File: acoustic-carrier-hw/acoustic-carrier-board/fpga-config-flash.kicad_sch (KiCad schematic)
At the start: 20 parts, among them IC1 ECP5-BGA256, J701 Conn_01x10_Socket, J702 Conn_01x08_Socket, U701 W25Q128JVS, U702 W25Q128JVS

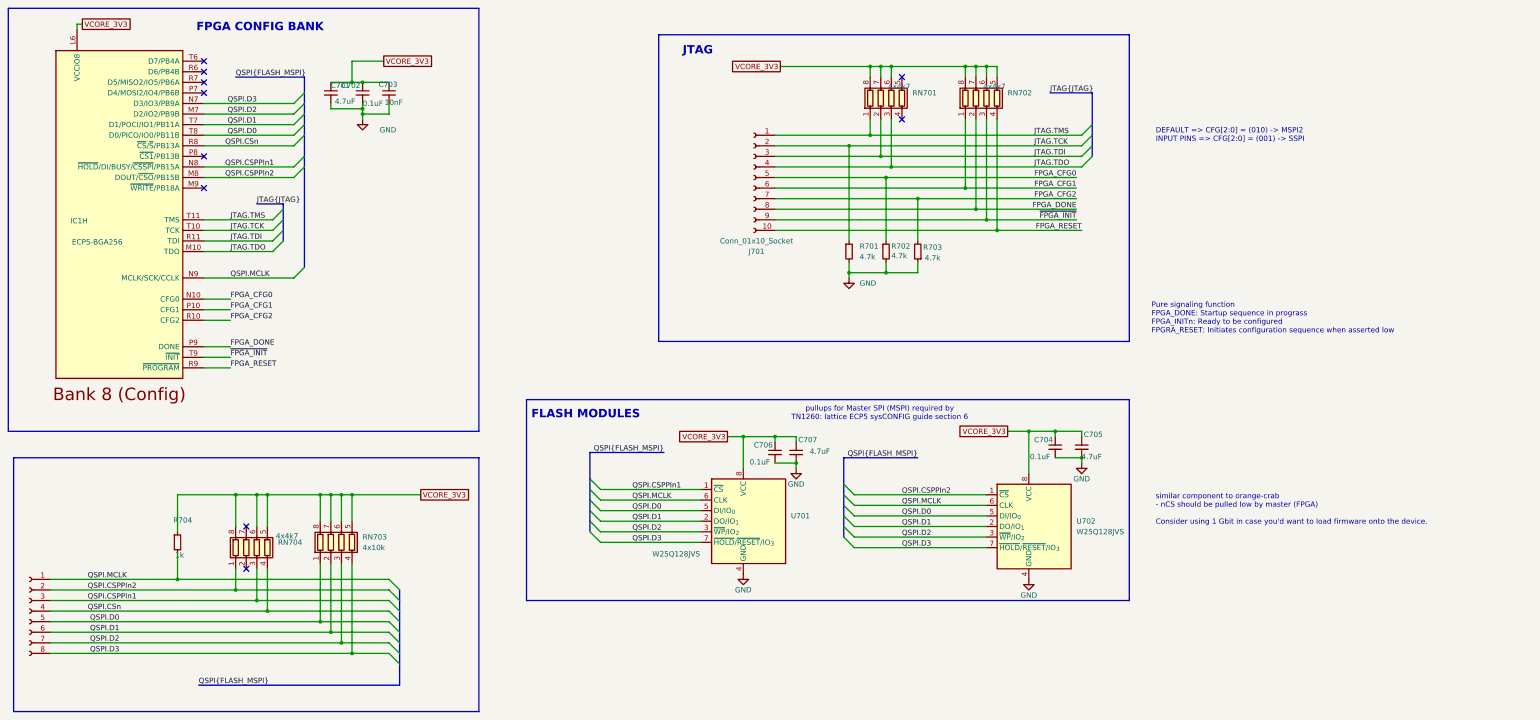
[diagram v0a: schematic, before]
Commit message: [carrier] Layout more or less complete (next) think about adding 6x2 connectors, and add extra pin signals to the connector for testing
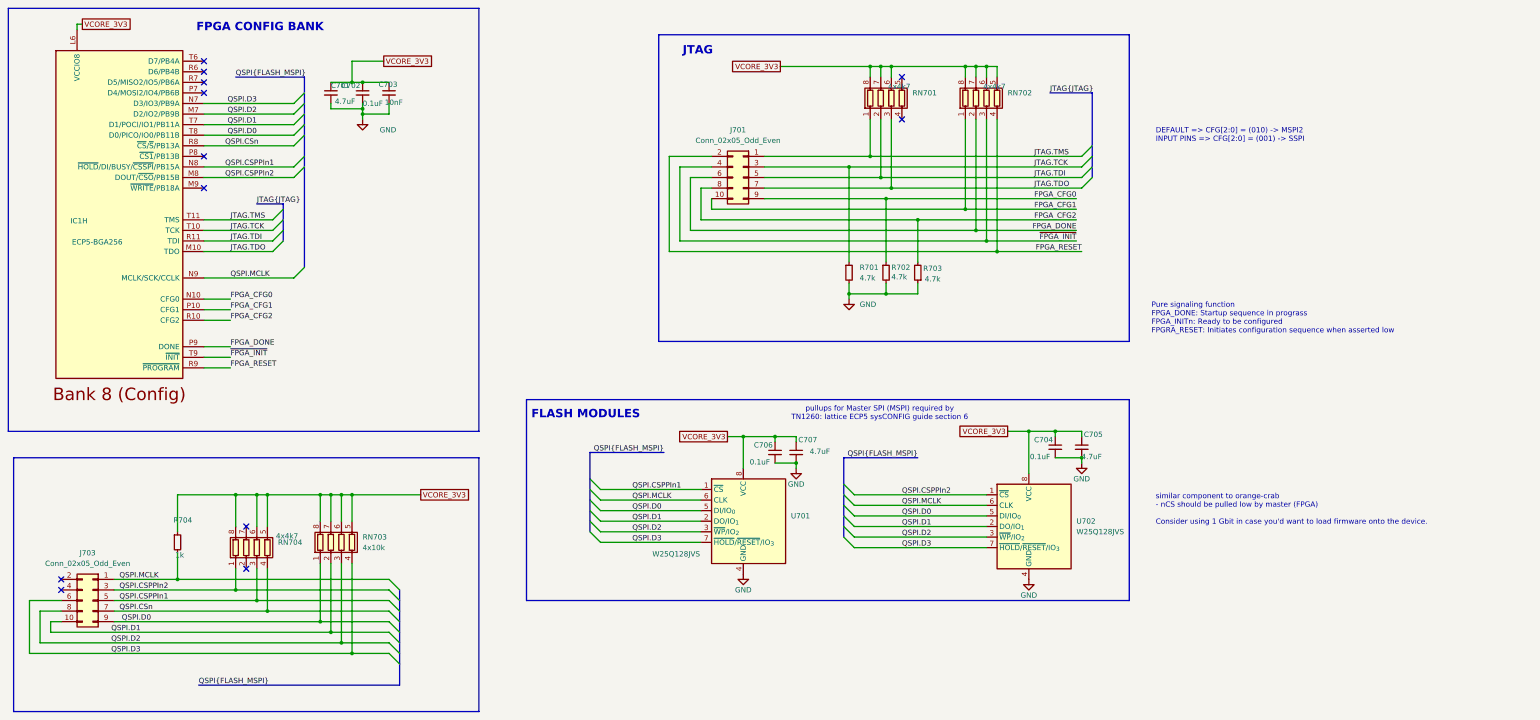
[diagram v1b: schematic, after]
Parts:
- removed J701: Conn_01x10_Socket, Connector_PinSocket_2.54mm:PinSocket_1x10_P2.54mm_Horizontal, symbol Connector:Conn_01x10_Socket
- removed J702: Conn_01x08_Socket, Connector_PinSocket_2.54mm:PinSocket_1x08_P2.54mm_Horizontal, symbol Connector:Conn_01x08_Socket
- added J701, J703: Conn_02x05_Odd_Even, Connector_PinSocket_2.54mm:PinSocket_2x05_P2.54mm_Horizontal, symbol Connector_Generic:Conn_02x05_Odd_Even
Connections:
- net FPGA_CFG0: now also J701.9 (Pin_9)
- net FPGA_CFG1: now also J701.10 (Pin_10)
- net FPGA_CFG2: now also J701.8 (Pin_8)
- net FPGA_DONE: now also J701.6 (Pin_6)
- net FPGA_RESET: now also J701.2 (Pin_2)
- net JTAG.TCK: now also J701.3 (Pin_3)
- net JTAG.TDI: now also J701.5 (Pin_5)
- net JTAG.TDO: now also J701.7 (Pin_7)
- net JTAG.TMS: now also J701.1 (Pin_1)
- net QSPI.CSPPIn1: now also J703.5 (Pin_5)
- net QSPI.CSPPIn2: now also J703.3 (Pin_3)
- net QSPI.CSn: now also J703.7 (Pin_7)
- net QSPI.D0: now also J703.9 (Pin_9)
- net QSPI.D1: now also J703.10 (Pin_10)
- net QSPI.D2: now also J703.8 (Pin_8)
- net QSPI.D3: now also J703.6 (Pin_6)
- net QSPI.MCLK: now also J703.1 (Pin_1)
- net ~{FPGA_INIT}: now also J701.4 (Pin_4)
- no-connect marks 10 -> 12
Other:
- moved on the sheet: R701, R702, R703

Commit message: [carrier] Added testpoints to rj45, added 6xx2 connectors (next) start routing the digital section
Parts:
- removed J701, J703: Conn_02x05_Odd_Even, Connector_PinSocket_2.54mm:PinSocket_2x05_P2.54mm_Horizontal, symbol Connector_Generic:Conn_02x05_Odd_Even
- added J701, J703: Conn_02x06_Odd_Even, Connector_PinSocket_2.54mm:PinSocket_2x06_P2.54mm_Horizontal, symbol Connector_Generic:Conn_02x06_Odd_Even
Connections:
- net FPGA_CFG0: now also J701.12 (Pin_12)
- net FPGA_CFG1: now also J701.11 (Pin_11)
- net FPGA_CFG2: now also J701.9 (Pin_9)
- net FPGA_DONE: now also J701.7 (Pin_7)
- net FPGA_RESET: now also J701.3 (Pin_3)
- net JTAG.TCK: now also J701.6 (Pin_6)
- net JTAG.TDI: now also J701.8 (Pin_8)
- net JTAG.TDO: now also J701.10 (Pin_10)
- net JTAG.TMS: now also J701.4 (Pin_4)
- net QSPI.CSPPIn1: now also J703.8 (Pin_8)
- net QSPI.CSPPIn2: now also J703.6 (Pin_6)
- net QSPI.CSn: now also J703.10 (Pin_10)
- net QSPI.D0: now also J703.12 (Pin_12)
- net QSPI.D1: now also J703.11 (Pin_11)
- net QSPI.D2: now also J703.9 (Pin_9)
- net QSPI.D3: now also J703.7 (Pin_7)
- net QSPI.MCLK: now also J703.4 (Pin_4)
- net ~{FPGA_INIT}: now also J701.5 (Pin_5)
- no-connect marks 12 -> 16
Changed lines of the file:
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@@
 	)
 	(no_connect
+		(at 39.37 151.13)
+	)
+	(no_connect
 		(at 26.67 156.21)
 	)
@@
 	)
 	(no_connect
+		(at 182.88 49.53)
+	)
+	(no_connect
 		(at 60.96 59.69)
 	)
@@
 	)
 	(no_connect
+		(at 195.58 49.53)
+	)
+	(no_connect
 		(at 228.6 43.18)
 	)
@@
 	)
 	(no_connect
+		(at 26.67 151.13)
+	)
+	(no_connect
 		(at 60.96 34.29)
 	)
@@
 	)
 	(symbol
-		(lib_id "Connector_Generic:Conn_02x05_Odd_Even")
-		(at 190.5 57.15 0)
-		(mirror y)
-		(unit 1)
-		(exclude_from_sim no)
-		(in_bom yes)
-		(on_board yes)
-		(dnp no)
-		(property "Reference" "J701"
-			(at 189.23 45.72 0)
-			(effects
-				(font
-					(size 1.27 1.27)
-				)
-			)
-		)
-		(property "Value" "Conn_02x05_Odd_Even"
-			(at 189.23 48.26 0)
-			(effects
-				(font
-					(size 1.27 1.27)
-				)
-			)
-		)
-		(property "Footprint" "Connector_PinSocket_2.54mm:PinSocket_2x05_P2.54mm_Horizontal"
-			(at 190.5 57.15 0)
-			(effects
-				(font
-					(size 1.27 1.27)
-				)
-				(hide yes)
-			)
-		)
-		(property "Datasheet" "https://jlcpcb.com/api/file/downloadByFileSystemAccessId/8588944816709242880"
-			(at 190.5 57.15 0)
-			(effects
-				(font
-					(size 1.27 1.27)
-				)
-				(hide yes)
-			)
-		)
-		(property "Description" "Generic connector, double row, 02x05, odd/even pin numbering scheme (row 1 odd numbers, row 2 even numbers), script generated (kicad-library-utils/schlib/autogen/connector/)"
-			(at 190.5 57.15 0)
-			(effects
-				(font
-					(size 1.27 1.27)
-				)
-				(hide yes)
-			)
-		)
-		(property "MPN" "PM254-2-05-W-8.5 "
-			(at 190.5 57.15 0)
-			(effects
-				(font
-					(size 1.27 1.27)
-				)
-				(hide yes)
-			)
-		)
-		(property "LPN" "C2897425"
-			(at 190.5 57.15 0)
-			(effects
-				(font
-					(size 1.27 1.27)
-				)
-				(hide yes)
-			)
-		)
-		(pin "6"
-		)
-		(pin "8"
-		)
-		(pin "3"
-		)
-		(pin "10"
-		)
-		(pin "5"
-		)
-		(pin "1"
-		)
-		(pin "7"
-		)
-		(pin "4"
-		)
-		(pin "2"
-		)
-		(pin "9"
-		)
-		(instances
-			(project "acoustic-carrier-board"
-				(path "/25b015c9-ab13-4427-b72c-b6f348597100/36da1f88-b4f8-4b81-86e1-fac0fb6202fa"
-					(reference "J701")
-					(unit 1)
-				)
-			)
-		)
-	)
-	(symbol
 		(lib_id "Device:C_Small")
 		(at 105.41 36.83 0)
@@
 	)
 	(symbol
+		(lib_id "Connector_Generic:Conn_02x06_Odd_Even")
+		(at 187.96 54.61 0)
+		(unit 1)
+		(exclude_from_sim no)
+		(in_bom yes)
+		(on_board yes)
+		(dnp no)
+		(fields_autoplaced yes)
+		(property "Reference" "J701"
+			(at 189.23 43.18 0)
+			(effects
+				(font
+					(size 1.27 1.27)
+				)
+			)
+		)
+		(property "Value" "Conn_02x06_Odd_Even"
+			(at 189.23 45.72 0)
+			(effects
+				(font
+					(size 1.27 1.27)
+				)
+			)
+		)
+		(property "Footprint" "Connector_PinSocket_2.54mm:PinSocket_2x06_P2.54mm_Horizontal"
+			(at 187.96 54.61 0)
+			(effects
+				(font
+					(size 1.27 1.27)
+				)
+				(hide yes)
+			)
+		)
+		(property "Datasheet" "~"
+			(at 187.96 54.61 0)
+			(effects
+				(font
+					(size 1.27 1.27)
+				)
+				(hide yes)
+			)
+		)
+		(property "Description" "Generic connector, double row, 02x06, odd/even pin numbering scheme (row 1 odd numbers, row 2 even numbers), script generated (kicad-library-utils/schlib/autogen/connector/)"
+			(at 187.96 54.61 0)
+			(effects
+				(font
+					(size 1.27 1.27)
+				)
+				(hide yes)
+			)
+		)
+		(property "LPN" "C2897426"
+			(at 187.96 54.61 0)
+			(effects
+				(font
+					(size 1.27 1.27)
+				)
+				(hide yes)
+			)
+		)
+		(property "MPN" "PM254-2-06-W-8.5 "
+			(at 187.96 54.61 0)
+			(effects
+				(font
+					(size 1.27 1.27)
+				)
+				(hide yes)
+			)
+		)
+		(pin "5"
+		)
+		(pin "11"
+		)
+		(pin "3"
+		)
+		(pin "7"
+		)
+		(pin "4"
+		)
+		(pin "10"
+		)
+		(pin "2"
+		)
+		(pin "9"
+		)
+		(pin "1"
+		)
+		(pin "6"
+		)
+		(pin "12"
+		)
+		(pin "8"
+		)
+		(instances
+			(project "acoustic-carrier-board"
+				(path "/25b015c9-ab13-4427-b72c-b6f348597100/36da1f88-b4f8-4b81-86e1-fac0fb6202fa"
+					(reference "J701")
+					(unit 1)
+				)
+			)
+		)
+	)
+	(symbol
 		(lib_id "Device:C_Small")
 		(at 198.12 123.19 0)
@@
 	)
 	(symbol
-		(lib_id "Connector_Generic:Conn_02x05_Odd_Even")
-		(at 34.29 158.75 0)
-		(mirror y)
-		(unit 1)
-		(exclude_from_sim no)
-		(in_bom yes)
-		(on_board yes)
-		(dnp no)
-		(property "Reference" "J703"
-			(at 33.02 147.32 0)
-			(effects
-				(font
-					(size 1.27 1.27)
-				)
-			)
-		)
-		(property "Value" "Conn_02x05_Odd_Even"
-			(at 33.02 149.86 0)
-			(effects
-				(font
-					(size 1.27 1.27)
-				)
-			)
-		)
-		(property "Footprint" "Connector_PinSocket_2.54mm:PinSocket_2x05_P2.54mm_Horizontal"
-			(at 34.29 158.75 0)
-			(effects
-				(font
-					(size 1.27 1.27)
-				)
-				(hide yes)
-			)
-		)
-		(property "Datasheet" "https://jlcpcb.com/api/file/downloadByFileSystemAccessId/8588944816709242880"
-			(at 34.29 158.75 0)
-			(effects
-				(font
-					(size 1.27 1.27)
-				)
-				(hide yes)
-			)
-		)
-		(property "Description" "Generic connector, double row, 02x05, odd/even pin numbering scheme (row 1 odd numbers, row 2 even numbers), script generated (kicad-library-utils/schlib/autogen/connector/)"
-			(at 34.29 158.75 0)
-			(effects
-				(font
-					(size 1.27 1.27)
-				)
-				(hide yes)
-			)
-		)
-		(property "MPN" "PM254-2-05-W-8.5 "
-			(at 34.29 158.75 0)
-			(effects
-				(font
-					(size 1.27 1.27)
-				)
-				(hide yes)
-			)
-		)
-		(property "LPN" "C2897425"
-			(at 34.29 158.75 0)
-			(effects
-				(font
-					(size 1.27 1.27)
-				)
-				(hide yes)
-			)
-		)
-		(pin "6"
-		)
-		(pin "8"
-		)
-		(pin "3"
-		)
-		(pin "10"
-		)
-		(pin "5"
-		)
-		(pin "1"
-		)
-		(pin "7"
-		)
-		(pin "4"
-		)
-		(pin "2"
-		)
-		(pin "9"
-		)
-		(instances
-			(project "acoustic-carrier-board"
-				(path "/25b015c9-ab13-4427-b72c-b6f348597100/36da1f88-b4f8-4b81-86e1-fac0fb6202fa"
-					(reference "J703")
-					(unit 1)
-				)
-			)
-		)
-	)
-	(symbol
 		(lib_id "Device:R_Small")
 		(at 54.61 144.78 0)
@@
 					(unit 1)
 				)
+			)
+		)
+	)
+	(symbol
+		(lib_id "Connector_Generic:Conn_02x06_Odd_Even")
+		(at 31.75 156.21 0)
+		(unit 1)
+		(exclude_from_sim no)
+		(in_bom yes)
+		(on_board yes)
+		(dnp no)
+		(fields_autoplaced yes)
+		(property "Reference" "J703"
+			(at 33.02 144.78 0)
+			(effects
+				(font
+					(size 1.27 1.27)
+				)
+			)
+		)
+		(property "Value" "Conn_02x06_Odd_Even"
+			(at 33.02 147.32 0)
+			(effects
+				(font
+					(size 1.27 1.27)
+				)
+			)
+		)
+		(property "Footprint" "Connector_PinSocket_2.54mm:PinSocket_2x06_P2.54mm_Horizontal"
+			(at 31.75 156.21 0)
+			(effects
+				(font
+					(size 1.27 1.27)
+				)
+				(hide yes)
+			)
+		)
+		(property "Datasheet" "~"
+			(at 31.75 156.21 0)
+			(effects
+				(font
+					(size 1.27 1.27)
+				)
+				(hide yes)
+			)
+		)
+		(property "Description" "Generic connector, double row, 02x06, odd/even pin numbering scheme (row 1 odd numbers, row 2 even numbers), script generated (kicad-library-utils/schlib/autogen/connector/)"
+			(at 31.75 156.21 0)
+			(effects
+				(font
+					(size 1.27 1.27)
+				)
+				(hide yes)
+			)
+		)
+		(property "LPN" "C2897426"
+			(at 31.75 156.21 0)
+			(effects
+				(font
+					(size 1.27 1.27)
+				)
+				(hide yes)
+			)
+		)
+		(property "MPN" "PM254-2-06-W-8.5 "
+			(at 31.75 156.21 0)
+			(effects
+				(font
+					(size 1.27 1.27)
+				)
+				(hide yes)
+			)
+		)
+		(pin "5"
+		)
+		(pin "11"
+		)
+		(pin "3"
+		)
+		(pin "7"
+		)
+		(pin "4"
+		)
+		(pin "10"
+		)
+		(pin "2"
+		)
+		(pin "9"
+		)
+		(pin "1"
+		)
+		(pin "6"
+		)
+		(pin "12"
+		)
+		(pin "8"
+		)
+		(instances
+			(project ""
+				(path "/25b015c9-ab13-4427-b72c-b6f348597100/36da1f88-b4f8-4b81-86e1-fac0fb6202fa"
+					(reference "J703")
+					(unit 1)
+				)
